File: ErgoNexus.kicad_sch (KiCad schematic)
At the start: 104 parts, among them J7 Conn_01x02, J8 Conn_01x02, SW1 SW_Push, SW2 RotaryEncoder_Switch, SW3 SW_Push, SW4 RotaryEncoder_Switch, U1 SuperMini nRF52840, U2 SuperMini nRF52840

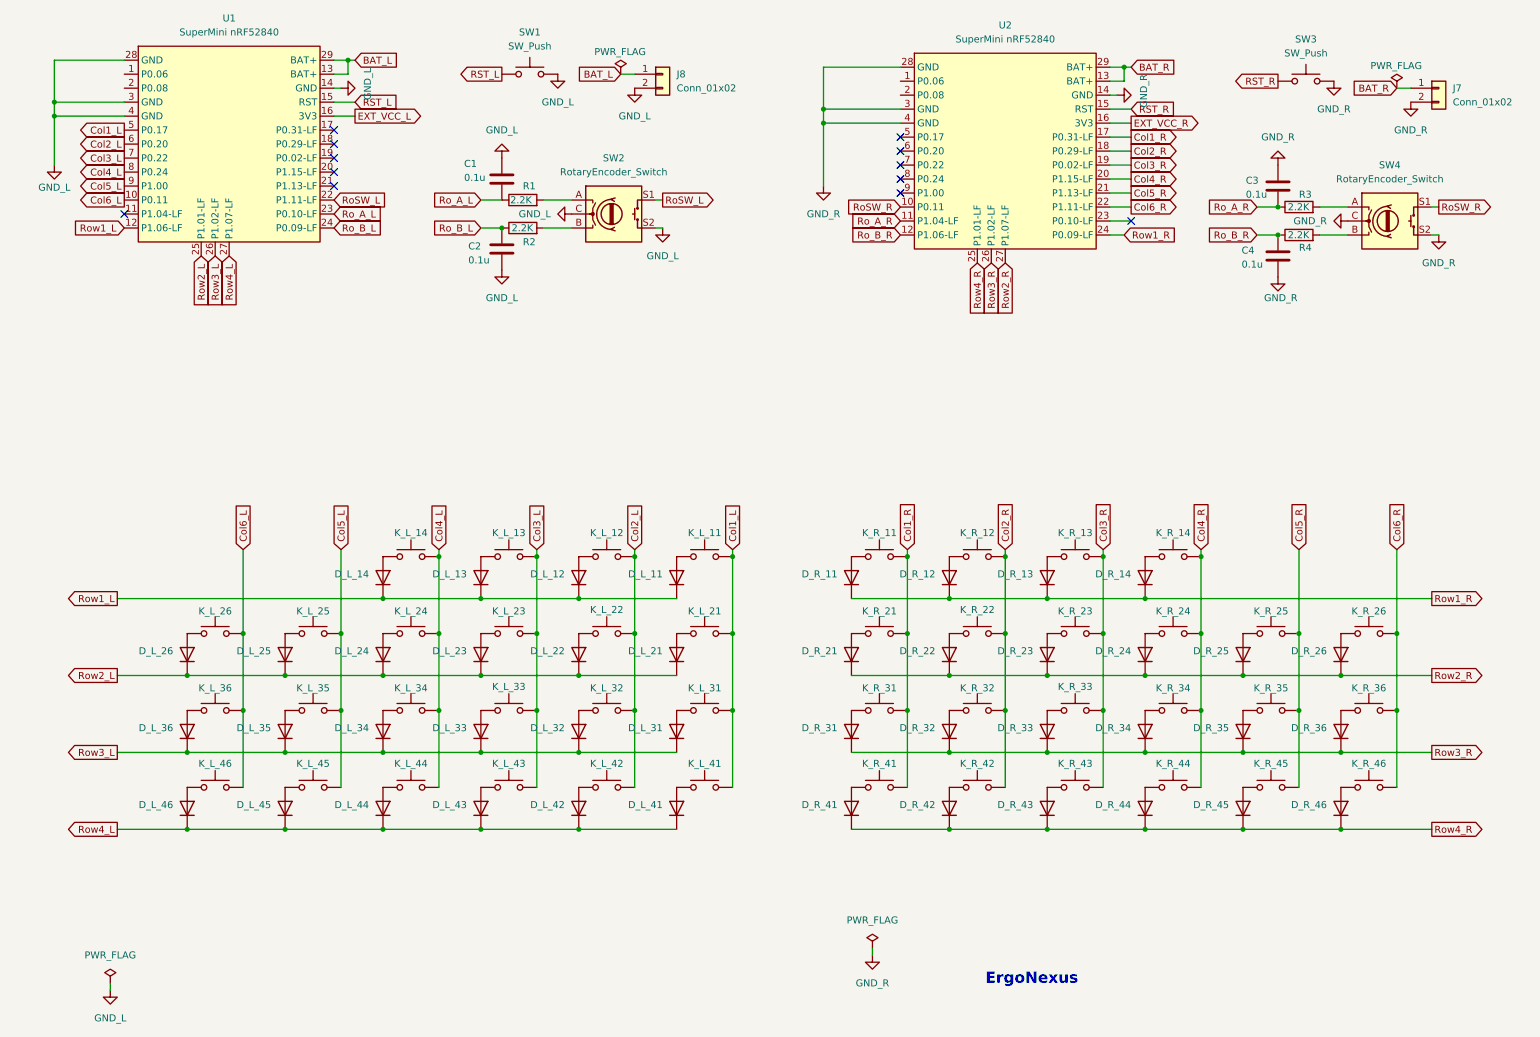
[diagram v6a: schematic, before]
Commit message: feat: 右側の配線完了
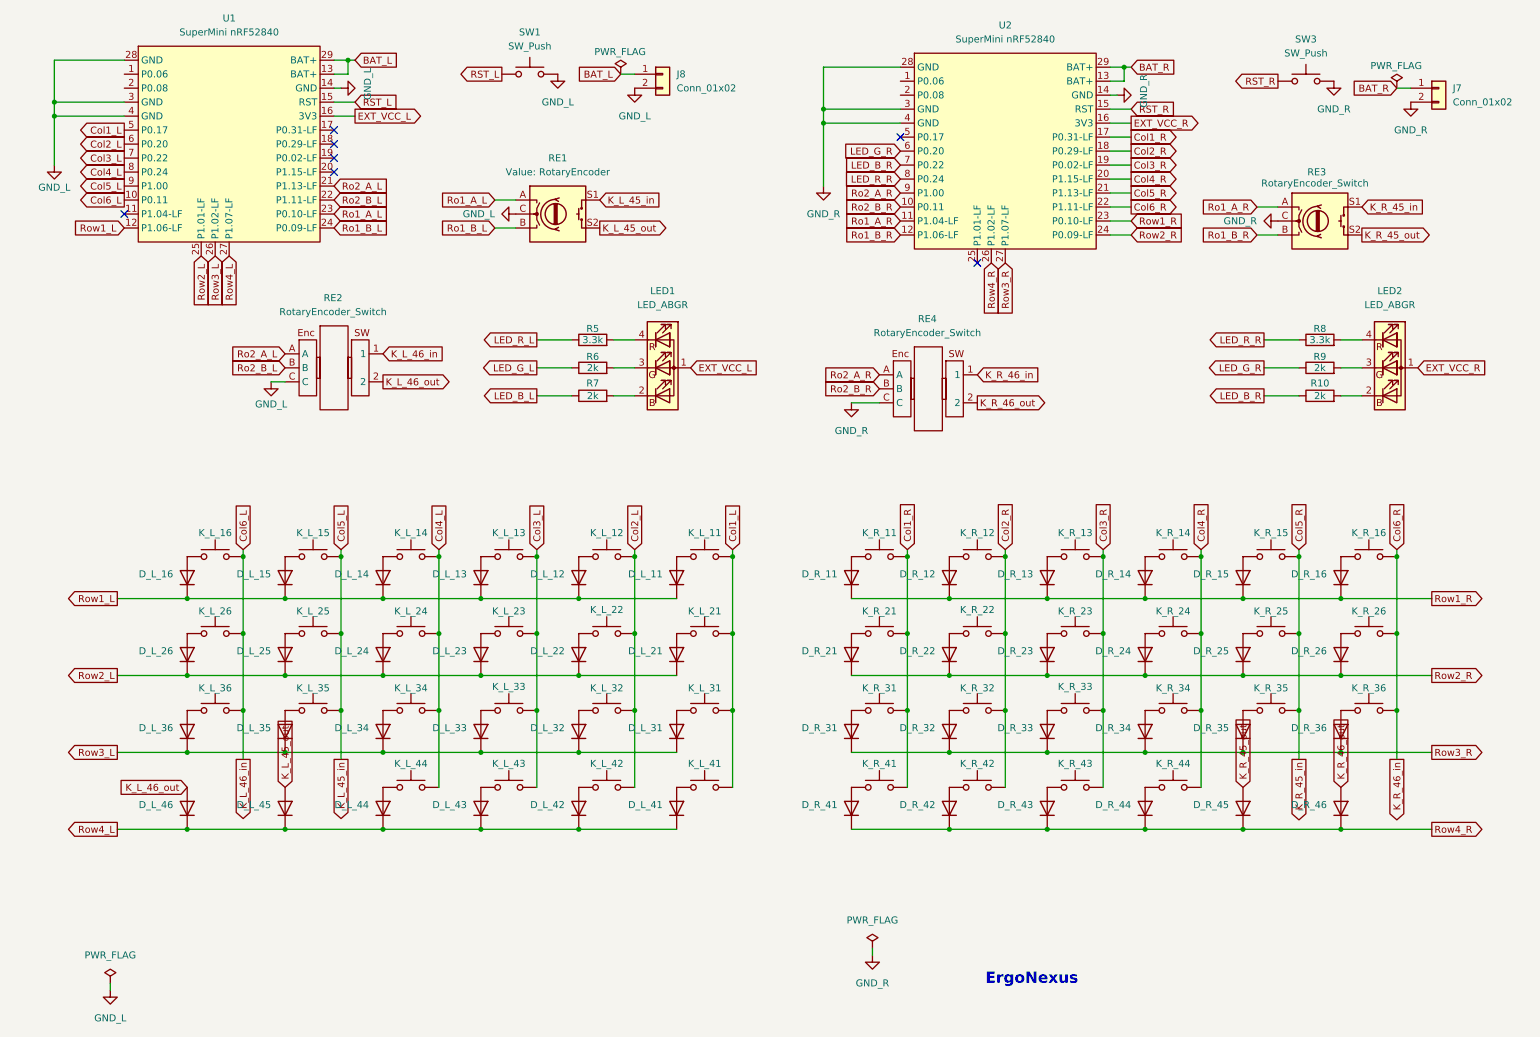
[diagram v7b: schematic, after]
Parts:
- removed C1, C2, C3, C4: 0.1u, Capacitor_THT:C_Disc_D3.8mm_W2.6mm_P2.50mm, symbol Device:C
- removed R1, R2, R3, R4: 2.2K, Keebio-Parts.pretty-master:Resistor-Compact-1-side, symbol Device:R
- added D_L_45, D_L_46, D_R_45, D_R_46: 1N4148SW, Diode_SMD:D_0402_1005Metric, symbol Diode:1N4148
- added LED1, LED2: LED_ABGR, mystster:LED Rectangle(OSTBMAZ2C1D), symbol Device:LED_ABGR
- added R10, R6, R7, R9: 2k, Keebio-Parts:R_0402, symbol Device:R
- added R5, R8: 3.3k, Keebio-Parts:R_0402, symbol Device:R
- added RE2, RE4: RotaryEncoder_Switch, THQWGD001:THQWGD001C [4pin] #1, symbol THQWGD001:THQWGD001_with_Click
- D_L_11, D_L_12, D_L_13, D_L_14, D_L_21, D_L_22, D_L_23, D_L_24, D_L_25, D_L_26, D_L_31, D_L_32, D_L_33, D_L_34, D_L_35, D_L_36, D_L_41, D_L_42, D_L_43, D_L_44, D_R_11, D_R_12, D_R_13, D_R_14, D_R_21, D_R_22, D_R_23, D_R_24, D_R_25, D_R_26, D_R_31, D_R_32, D_R_33, D_R_34, D_R_35, D_R_36, D_R_41, D_R_42, D_R_43, D_R_44: value 1N4148 -> 1N4148SW; footprint kbd_Parts:Diode_TH_SMD -> Diode_SMD:D_0402_1005Metric
- D_L_15: renamed from D_L_45; value 1N4148 -> 1N4148SW; footprint kbd_Parts:Diode_TH_SMD -> Diode_SMD:D_0402_1005Metric
- D_L_16: renamed from D_L_46; value 1N4148 -> 1N4148SW; footprint kbd_Parts:Diode_TH_SMD -> Diode_SMD:D_0402_1005Metric
- D_R_15: renamed from D_R_45; value 1N4148 -> 1N4148SW; footprint kbd_Parts:Diode_TH_SMD -> Diode_SMD:D_0402_1005Metric
- D_R_16: renamed from D_R_46; value 1N4148 -> 1N4148SW; footprint kbd_Parts:Diode_TH_SMD -> Diode_SMD:D_0402_1005Metric
- RE1: renamed from SW2; value RotaryEncoder_Switch -> RotaryEncoder
- renumbered K_L_45 to K_L_15, K_L_46 to K_L_16, K_R_45 to K_R_15, K_R_46 to K_R_16, SW4 to RE3
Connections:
- net Ro_A_L is gone; now on net Ro1_A_L: U1.23 (P0.10-LF)
- net Ro_A_R is gone; now on net Ro1_A_R: U2.11 (P1.04-LF)
- net Ro_B_L is gone; now on net Ro1_B_L: U1.24 (P0.09-LF)
- net Ro_B_R is gone; now on net Ro1_B_R: U2.12 (P1.06-LF)
- net Col5_L: now also RE1.S1
- net Col5_R: now also RE3.S1
- net Col6_L: now also RE2.1
- net Col6_R: now also RE4.1
- net EXT_VCC_L: now also LED1.1 (A)
- net EXT_VCC_R: now also LED2.1 (A)
- net GND_L: now also RE2.C; no longer RE1.S2
- net GND_R: now also RE4.C; no longer RE3.S2
- net Row1_L: now also D_L_15.1 (K), D_L_16.1 (K)
- net Row1_R: now also D_R_15.1 (K), D_R_16.1 (K), U2.23 (P0.10-LF); no longer U2.24 (P0.09-LF)
- net Row2_R: now also U2.24 (P0.09-LF); no longer U2.27 (P1.07-LF)
- net Row3_R: now also U2.27 (P1.07-LF); no longer U2.26 (P1.02-LF)
- net Row4_L: now also D_L_45.1 (K), D_L_46.1 (K); no longer D_L_15.1 (K), D_L_16.1 (K)
- net Row4_R: now also U2.26 (P1.02-LF), D_R_45.1 (K), D_R_46.1 (K); no longer D_R_15.1 (K), D_R_16.1 (K), U2.25 (P1.01-LF)
- net Ro1_A_R: now reaches RE3.A
- net Ro1_B_R: now reaches RE3.B
- net Ro1_A_L: now reaches RE1.A
- net LED_G_R: now reaches U2.6 (P0.20)
- net LED_G_R: now also R9.1
- net LED_B_R: now reaches U2.7 (P0.22)
- net LED_B_R: now also R10.1
- net LED_R_R: now reaches U2.8 (P0.24)
- net LED_R_R: now also R8.1
- net Ro2_A_R: now reaches U2.9 (P1.00)
- net Ro2_A_R: now also RE4.A
- net Ro1_B_L: now reaches RE1.B
- net Ro2_A_L: now reaches U1.21 (P1.13-LF)
- net Ro2_A_L: now also RE2.A
- net RoSW_L renamed Ro2_B_L
- net Ro2_B_L: now also RE2.B; no longer RE1.S1
- net RoSW_R renamed Ro2_B_R
- net Ro2_B_R: now also RE4.B; no longer RE3.S1
- new net: LED1.3 (GK), R6.2
- new net: LED2.2 (BK), R10.2
- new net: LED2.4 (RK), R8.2
- new net: LED2.3 (GK), R9.2
- new net: LED1.2 (BK), R7.2
- new net: LED1.4 (RK), R5.2
- new net K_L_45_out: D_L_45.2 (A), RE1.S2
- new net K_L_46_out: D_L_46.2 (A), RE2.2
- new net K_R_45_out: D_R_45.2 (A), RE3.S2
- new net K_R_46_out: D_R_46.2 (A), RE4.2
- new net LED_B_L: R7.1
- new net LED_G_L: R6.1
- new net LED_R_L: R5.1
- no-connect marks 12 -> 7
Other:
- moved on the sheet: D_L_15, D_L_16, D_R_15, D_R_16, K_L_15, K_L_16, K_R_15, K_R_16, RE1, RE3

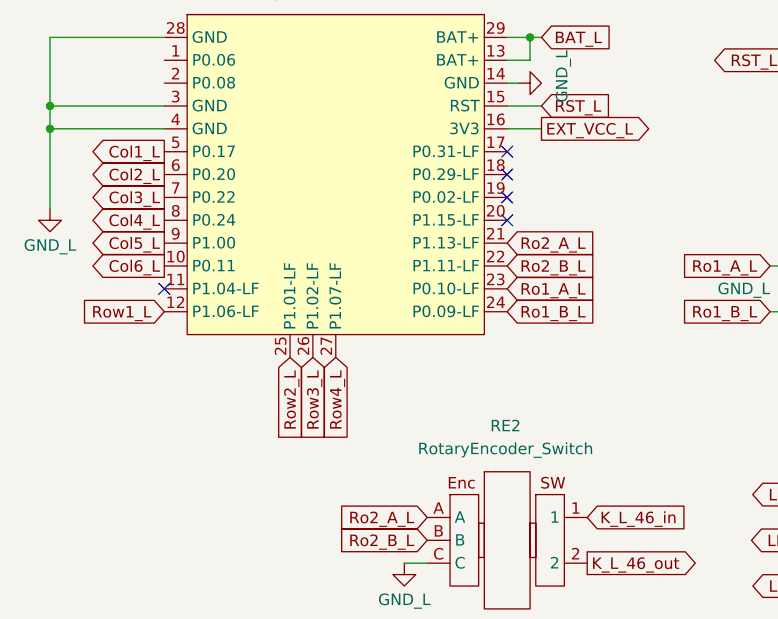
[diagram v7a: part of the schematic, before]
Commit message: feat: 左側の配線が完了
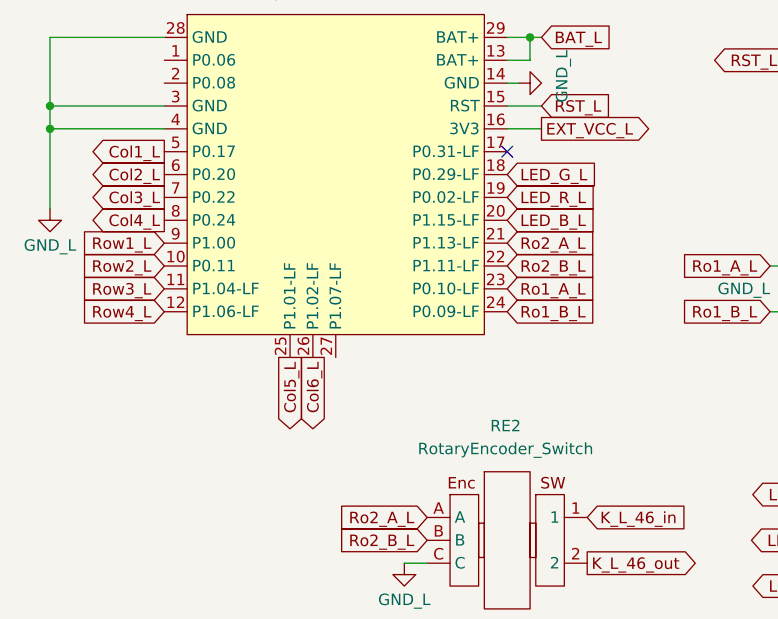
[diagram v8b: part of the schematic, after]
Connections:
- net Col5_L: now also U1.25 (P1.01-LF); no longer U1.9 (P1.00)
- net Col6_L: now also U1.26 (P1.02-LF); no longer U1.10 (P0.11)
- net LED_B_L: now also U1.20 (P1.15-LF)
- net LED_G_L: now also U1.18 (P0.29-LF)
- net LED_R_L: now also U1.19 (P0.02-LF)
- net Row1_L: now also U1.9 (P1.00); no longer U1.12 (P1.06-LF)
- net Row2_L: now also U1.10 (P0.11); no longer U1.25 (P1.01-LF)
- net Row3_L: now also U1.11 (P1.04-LF); no longer U1.26 (P1.02-LF)
- net Row4_L: now also U1.12 (P1.06-LF); no longer U1.27 (P1.07-LF)
- no-connect marks 7 -> 3
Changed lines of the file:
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@@
 	)
 	(no_connect
-		(at 67.31 38.1)
-	)
-	(no_connect
 		(at 67.31 35.56)
 	)
 	(no_connect
-		(at 67.31 40.64)
-	)
-	(no_connect
-		(at 29.21 50.8)
-	)
-	(no_connect
 		(at 170.18 36.83)
 	)
-	(no_connect
-		(at 67.31 43.18)
-	)
 	(wire
 		(pts
@@
 	(global_label "Row1_L"
 		(shape input)
-		(at 29.21 53.34 180)
+		(at 29.21 45.72 180)
 		(fields_autoplaced yes)
 		(effects
@@
 		)
 		(property "Intersheetrefs" "${INTERSHEET_REFS}"
-			(at 19.2701 53.34 0)
+			(at 19.2701 45.72 0)
 			(hide yes)
 			(show_name no)
@@
 	(global_label "Col5_L"
 		(shape output)
-		(at 29.21 45.72 180)
+		(at 43.18 58.42 270)
 		(fields_autoplaced yes)
 		(effects
@@
 		)
 		(property "Intersheetrefs" "${INTERSHEET_REFS}"
-			(at 38.4846 45.72 0)
+			(at 43.18 67.6946 90)
 			(hide yes)
 			(show_name no)
@@
 					(size 1.27 1.27)
 				)
-				(justify left)
+				(justify right)
 			)
 		)
@@
 		)
 	)
+	(global_label "LED_G_L"
+		(shape input)
+		(at 67.31 38.1 0)
+		(fields_autoplaced yes)
+		(effects
+			(font
+				(size 1.27 1.27)
+			)
+			(justify left)
+		)
+		(property "Intersheetrefs" "${INTERSHEET_REFS}"
+			(at 77.9756 38.1 0)
+			(hide yes)
+			(show_name no)
+			(do_not_autoplace no)
+			(effects
+				(font
+					(size 1.27 1.27)
+				)
+				(justify left)
+			)
+		)
+	)
 	(global_label "Col3_L"
 		(shape input)
@@
 		)
 	)
+	(global_label "LED_R_L"
+		(shape input)
+		(at 67.31 40.64 0)
+		(fields_autoplaced yes)
+		(effects
+			(font
+				(size 1.27 1.27)
+			)
+			(justify left)
+		)
+		(property "Intersheetrefs" "${INTERSHEET_REFS}"
+			(at 77.9756 40.64 0)
+			(hide yes)
+			(show_name no)
+			(do_not_autoplace no)
+			(effects
+				(font
+					(size 1.27 1.27)
+				)
+				(justify left)
+			)
+		)
+	)
 	(global_label "Row4_L"
 		(shape input)
-		(at 48.26 58.42 270)
+		(at 29.21 53.34 180)
 		(fields_autoplaced yes)
 		(effects
@@
 		)
 		(property "Intersheetrefs" "${INTERSHEET_REFS}"
-			(at 48.26 68.3599 90)
+			(at 19.2701 53.34 0)
 			(hide yes)
 			(show_name no)
@@
 		)
 	)
+	(global_label "LED_B_L"
+		(shape input)
+		(at 67.31 43.18 0)
+		(fields_autoplaced yes)
+		(effects
+			(font
+				(size 1.27 1.27)
+			)
+			(justify left)
+		)
+		(property "Intersheetrefs" "${INTERSHEET_REFS}"
+			(at 77.9756 43.18 0)
+			(hide yes)
+			(show_name no)
+			(do_not_autoplace no)
+			(effects
+				(font
+					(size 1.27 1.27)
+				)
+				(justify left)
+			)
+		)
+	)
 	(global_label "Col2_L"
 		(shape input)
@@
 	(global_label "Row2_L"
 		(shape input)
-		(at 43.18 58.42 270)
+		(at 29.21 48.26 180)
 		(fields_autoplaced yes)
 		(effects
@@
 		)
 		(property "Intersheetrefs" "${INTERSHEET_REFS}"
-			(at 43.18 68.3599 90)
+			(at 19.2701 48.26 0)
 			(hide yes)
 			(show_name no)
@@
 	(global_label "Col6_L"
 		(shape output)
-		(at 29.21 48.26 180)
+		(at 45.72 58.42 270)
 		(fields_autoplaced yes)
 		(effects
@@
 		)
 		(property "Intersheetrefs" "${INTERSHEET_REFS}"
-			(at 19.9354 48.26 0)
+			(at 45.72 67.6946 90)
 			(hide yes)
 			(show_name no)
@@
 	(global_label "Row3_L"
 		(shape input)
-		(at 45.72 58.42 270)
+		(at 29.21 50.8 180)
 		(fields_autoplaced yes)
 		(effects
@@
 		)
 		(property "Intersheetrefs" "${INTERSHEET_REFS}"
-			(at 45.72 68.3599 90)
+			(at 19.2701 50.8 0)
 			(hide yes)
 			(show_name no)
